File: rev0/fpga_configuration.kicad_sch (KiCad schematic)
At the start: 40 parts, among them IC1 ECP5-BGA256, J10 TC_SWD, J5 Conn_FPGA_JTAG_10, J6 Conn_ARM_JTAG_SWD_10, U6 ATSAMD11D14A-MUT, U7 W25Q32JVSS

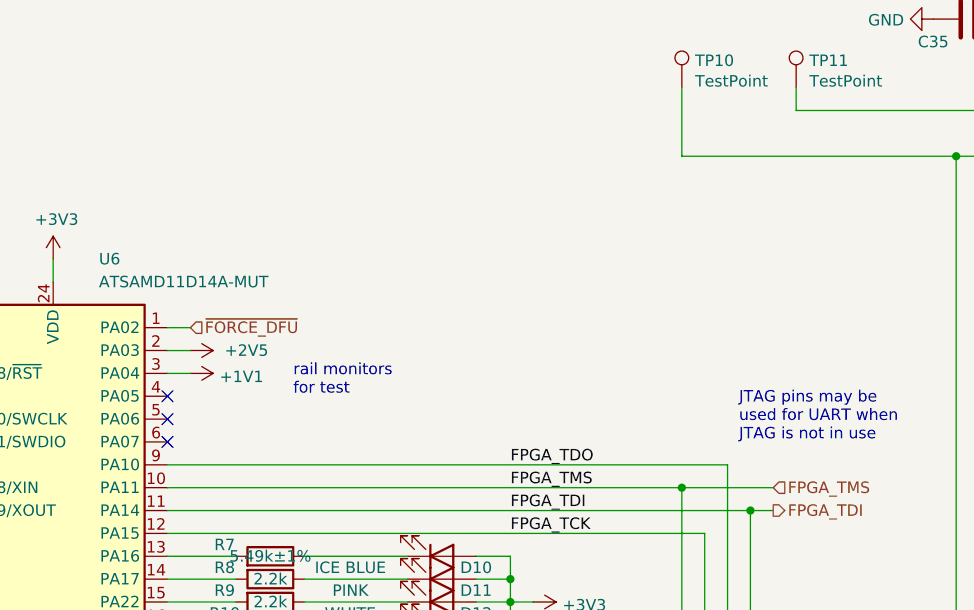
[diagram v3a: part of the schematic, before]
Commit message: hardware: add pin strap for version detection
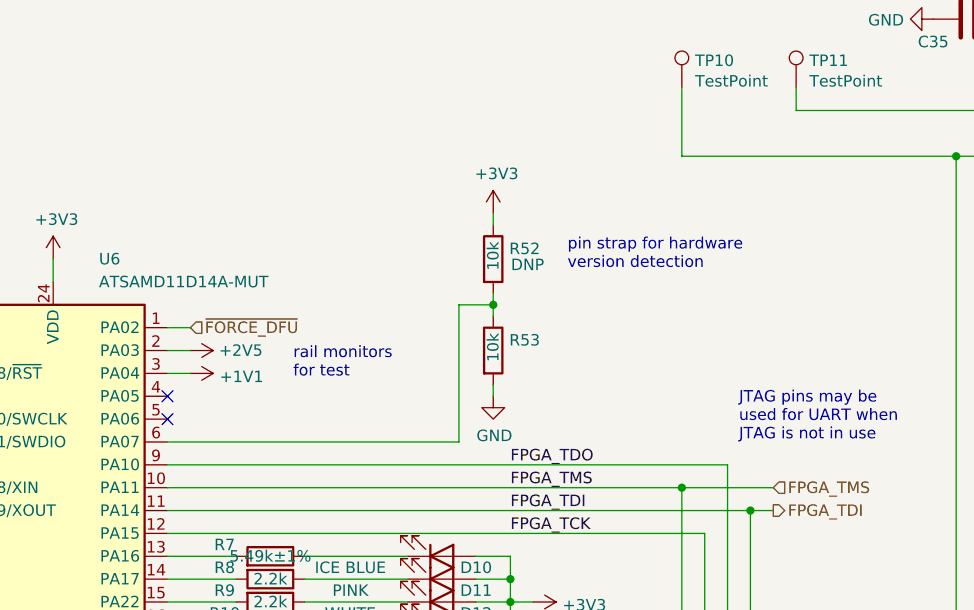
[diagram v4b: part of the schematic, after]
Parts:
- added R52, R53: 10k, Resistor_SMD:R_0402_1005Metric, symbol Device:R
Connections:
- net +3V3: now also R52.1
- net GND: now also R53.2
- net at U6.6 (PA07): now also R52.2, R53.1
- no-connect marks 13 -> 12
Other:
- note added: "pin strap for hardware version detection"
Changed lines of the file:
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@@
   (junction (at 195.58 35.56) (diameter 0) (color 0 0 0 0)
+  )
+  (junction (at 141.605 57.15) (diameter 0) (color 0 0 0 0)
   )
   (junction (at 138.43 187.96) (diameter 0) (color 0 0 0 0)
@@
   (no_connect (at 247.65 73.66))
   (no_connect (at 50.8 173.99))
-  (no_connect (at 105.41 72.39))
   (no_connect (at 50.8 176.53))
   (no_connect (at 123.19 162.56))
@@
     (stroke (width 0) (type default) (color 0 0 0 0))
   )
+  (wire (pts (xy 141.605 67.31) (xy 141.605 66.04))
+    (stroke (width 0) (type default) (color 0 0 0 0))
+  )
   (wire (pts (xy 64.77 107.95) (xy 64.77 110.49))
     (stroke (width 0) (type default) (color 0 0 0 0))
@@
     (stroke (width 0) (type default) (color 0 0 0 0))
   )
+  (wire (pts (xy 141.605 48.26) (xy 141.605 46.99))
+    (stroke (width 0) (type default) (color 0 0 0 0))
+  )
   (wire (pts (xy 92.71 52.07) (xy 92.71 54.61))
     (stroke (width 0) (type default) (color 0 0 0 0))
@@
     (stroke (width 0) (type default) (color 0 0 0 0))
   )
+  (wire (pts (xy 137.795 72.39) (xy 105.41 72.39))
+    (stroke (width 0) (type default) (color 0 0 0 0))
+  )
   (wire (pts (xy 105.41 90.17) (xy 113.03 90.17))
     (stroke (width 0) (type default) (color 0 0 0 0))
@@
     (stroke (width 0) (type default) (color 0 0 0 0))
   )
+  (wire (pts (xy 141.605 57.15) (xy 141.605 55.88))
+    (stroke (width 0) (type default) (color 0 0 0 0))
+  )
   (wire (pts (xy 233.68 128.27) (xy 247.65 128.27))
     (stroke (width 0) (type default) (color 0 0 0 0))
@@
     (stroke (width 0) (type default) (color 0 0 0 0))
   )
+  (wire (pts (xy 141.605 58.42) (xy 141.605 57.15))
+    (stroke (width 0) (type default) (color 0 0 0 0))
+  )
   (wire (pts (xy 71.12 36.83) (xy 71.12 39.37))
     (stroke (width 0) (type default) (color 0 0 0 0))
@@
     (stroke (width 0) (type default) (color 0 0 0 0))
   )
+  (wire (pts (xy 137.795 57.15) (xy 137.795 72.39))
+    (stroke (width 0) (type default) (color 0 0 0 0))
+  )
   (wire (pts (xy 33.02 171.45) (xy 50.8 171.45))
     (stroke (width 0) (type default) (color 0 0 0 0))
@@
   )
   (wire (pts (xy 33.02 62.23) (xy 33.02 64.77))
+    (stroke (width 0) (type default) (color 0 0 0 0))
+  )
+  (wire (pts (xy 141.605 57.15) (xy 137.795 57.15))
     (stroke (width 0) (type default) (color 0 0 0 0))
   )
@@
     (effects (font (size 1.27 1.27)) (justify left bottom))
   )
-  (text "rail monitors\nfor test" (at 119.38 67.31 0)
+  (text "rail monitors\nfor test" (at 119.38 65.405 0)
+    (effects (font (size 1.27 1.27)) (justify left bottom))
+  )
+  (text "pin strap for hardware\nversion detection" (at 149.86 53.34 0)
     (effects (font (size 1.27 1.27)) (justify left bottom))
   )
@@
       (effects (font (size 1.27 1.27)) hide)
     )
-    (property "Value" "+2V5" (id 1) (at 111.76 62.23 90)
+    (property "Value" "+2V5" (id 1) (at 111.125 62.23 90)
       (effects (font (size 1.27 1.27)) (justify left))
     )
@@
     (pin "1")
   )
+  (symbol (lib_id "power:+3V3") (at 141.605 46.99 0) (unit 1)
+    (in_bom yes) (on_board yes)
+    (property "Reference" "#PWR0138" (id 0) (at 141.605 50.8 0)
+      (effects (font (size 1.27 1.27)) hide)
+    )
+    (property "Value" "+3V3" (id 1) (at 141.986 42.5958 0))
+    (property "Footprint" "" (id 2) (at 141.605 46.99 0)
+      (effects (font (size 1.27 1.27)) hide)
+    )
+    (property "Datasheet" "" (id 3) (at 141.605 46.99 0)
+      (effects (font (size 1.27 1.27)) hide)
+    )
+    (pin "1")
+  )
+  (symbol (lib_id "power:GND") (at 141.605 67.31 0) (unit 1)
+    (in_bom yes) (on_board yes)
+    (property "Reference" "#PWR0139" (id 0) (at 141.605 73.66 0)
+      (effects (font (size 1.27 1.27)) hide)
+    )
+    (property "Value" "GND" (id 1) (at 141.732 71.7042 0))
+    (property "Footprint" "" (id 2) (at 141.605 67.31 0)
+      (effects (font (size 1.27 1.27)) hide)
+    )
+    (property "Datasheet" "" (id 3) (at 141.605 67.31 0)
+      (effects (font (size 1.27 1.27)) hide)
+    )
+    (pin "1")
+  )
+  (symbol (lib_id "Device:R") (at 141.605 62.23 0) (unit 1)
+    (in_bom yes) (on_board yes)
+    (property "Reference" "R53" (id 0) (at 143.383 61.087 0)
+      (effects (font (size 1.27 1.27)) (justify left))
+    )
+    (property "Value" "10k" (id 1) (at 141.605 63.5 90)
+      (effects (font (size 1.27 1.27)) (justify left))
+    )
+    (property "Footprint" "Resistor_SMD:R_0402_1005Metric" (id 2) (at 139.827 62.23 90)
+      (effects (font (size 1.27 1.27)) hide)
+    )
+    (property "Datasheet" "~" (id 3) (at 141.605 62.23 0)
+      (effects (font (size 1.27 1.27)) hide)
+    )
+    (property "Part Number" "GENERIC-RES-0402-10K" (id 4) (at 141.605 62.23 0)
+      (effects (font (size 1.27 1.27)) hide)
+    )
+    (property "Substitution" "any equivalent" (id 5) (at 141.605 62.23 0)
+      (effects (font (size 1.27 1.27)) hide)
+    )
+    (pin "1")
+    (pin "2")
+  )
+  (symbol (lib_id "Device:R") (at 141.605 52.07 0) (unit 1)
+    (in_bom yes) (on_board yes)
+    (property "Reference" "R52" (id 0) (at 143.383 50.927 0)
+      (effects (font (size 1.27 1.27)) (justify left))
+    )
+    (property "Value" "10k" (id 1) (at 141.605 53.34 90)
+      (effects (font (size 1.27 1.27)) (justify left))
+    )
+    (property "Footprint" "Resistor_SMD:R_0402_1005Metric" (id 2) (at 139.827 52.07 90)
+      (effects (font (size 1.27 1.27)) hide)
+    )
+    (property "Datasheet" "~" (id 3) (at 141.605 52.07 0)
+      (effects (font (size 1.27 1.27)) hide)
+    )
+    (property "Part Number" "GENERIC-RES-0402-10K" (id 4) (at 141.605 52.07 0)
+      (effects (font (size 1.27 1.27)) hide)
+    )
+    (property "Substitution" "any equivalent" (id 5) (at 141.605 52.07 0)
+      (effects (font (size 1.27 1.27)) hide)
+    )
+    (property "DNP" "DNP" (id 6) (at 145.415 52.705 0))
+    (pin "1")
+    (pin "2")
+  )
 )

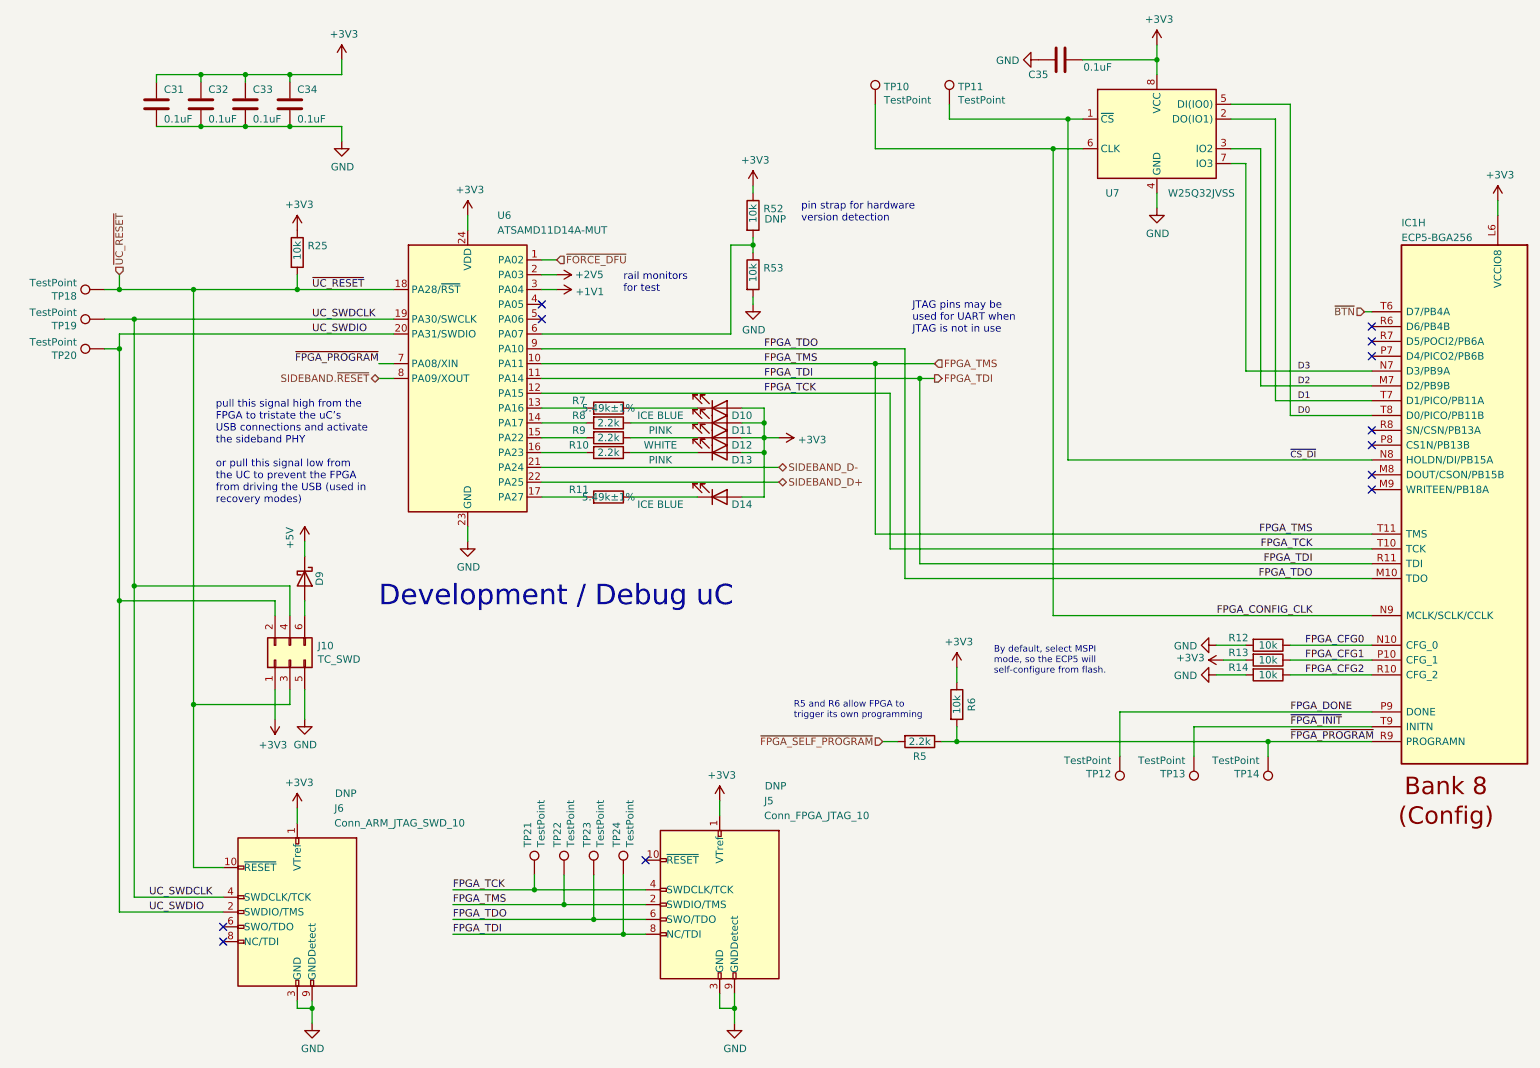
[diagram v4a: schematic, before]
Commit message: hardware: add FPGA interrupt
allows FPGA to signal that it has something to say to the
microcontroller
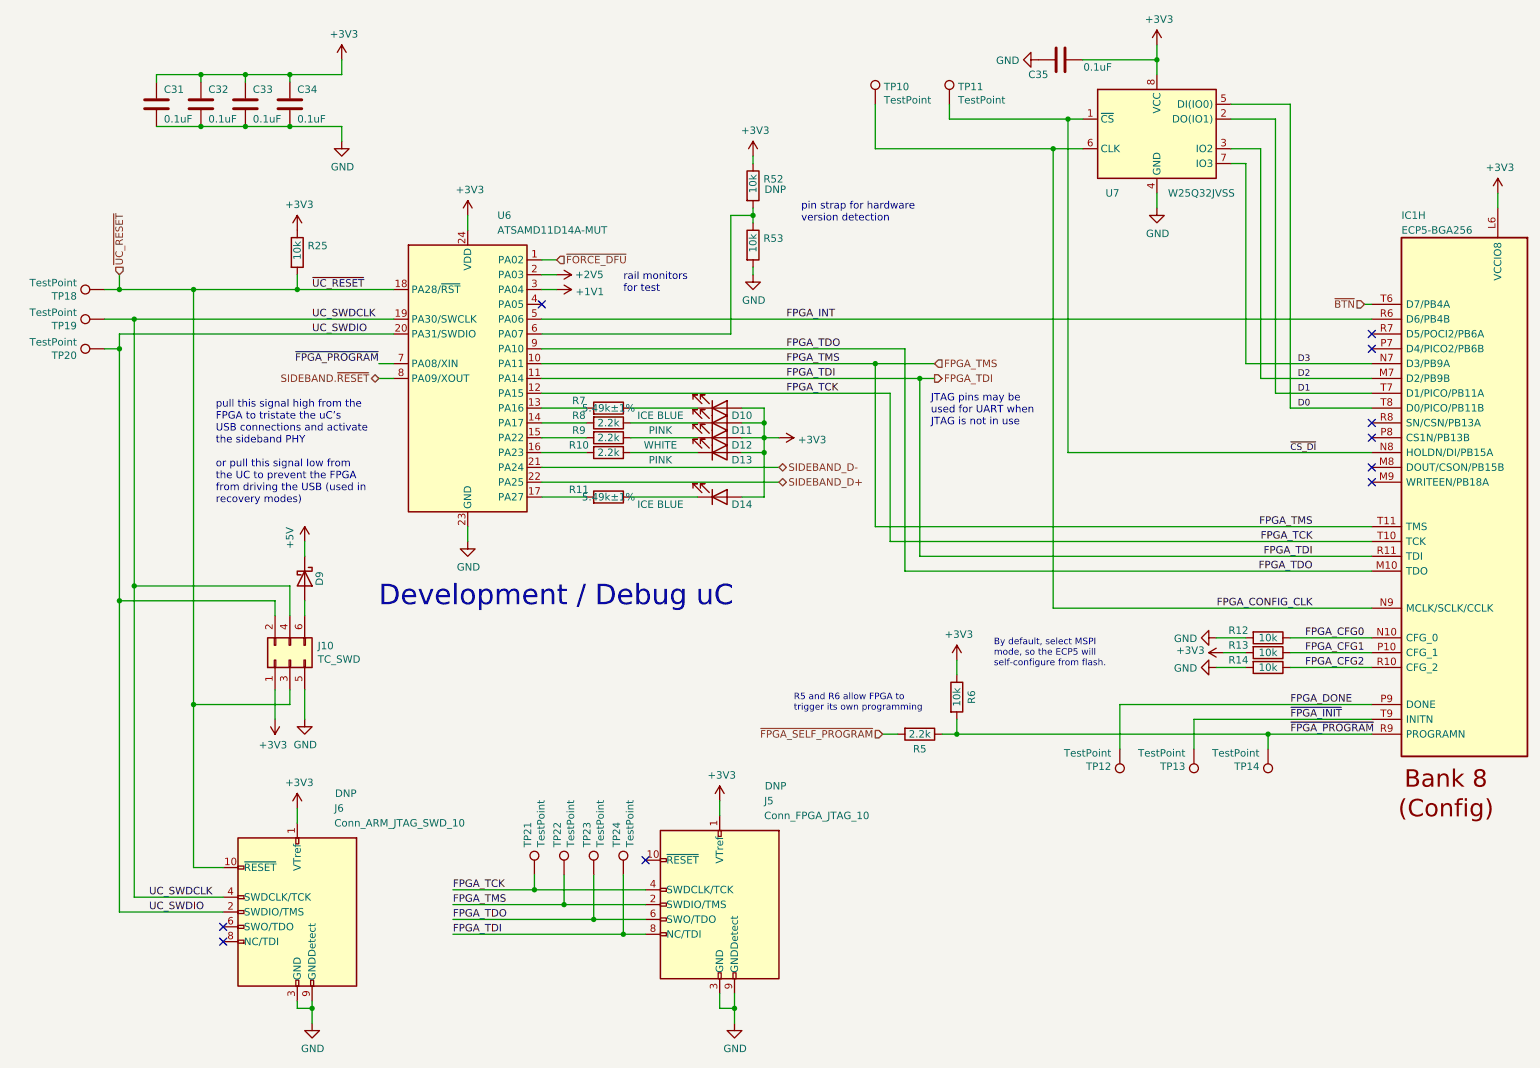
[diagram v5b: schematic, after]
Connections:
- net FPGA_INT: now reaches IC1.R6 (D6/PB4B)
- net FPGA_INT: now also U6.5 (PA06)
- no-connect marks 12 -> 10
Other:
- moved on the sheet: IC1H, R12, R13, R14, R5, R52, R53, R6, TP12, TP13, TP14

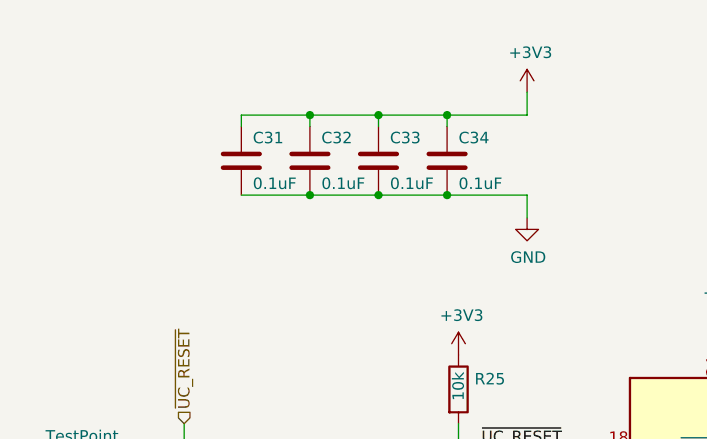
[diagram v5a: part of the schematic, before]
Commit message: hardware: restore 1.8 V RAM supply as an option
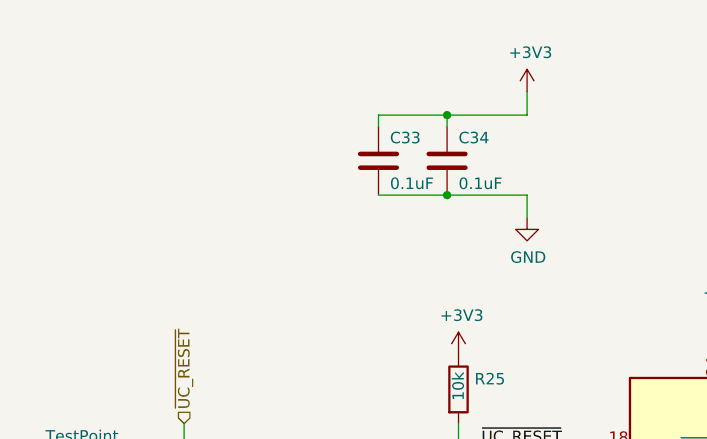
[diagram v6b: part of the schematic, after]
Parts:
- removed C31, C32: 0.1uF, Capacitor_SMD:C_0402_1005Metric, symbol Device:C
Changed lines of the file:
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@@
   (junction (at 229.87 140.97) (diameter 0) (color 0 0 0 0)
   )
-  (junction (at 54.61 36.83) (diameter 0) (color 0 0 0 0)
-  )
   (junction (at 33.02 64.77) (diameter 0) (color 0 0 0 0)
   )
@@
   (junction (at 33.02 118.11) (diameter 0) (color 0 0 0 0)
   )
-  (junction (at 46.99 36.83) (diameter 0) (color 0 0 0 0)
-  )
   (junction (at 210.82 25.4) (diameter 0) (color 0 0 0 0)
   )
   (junction (at 63.5 64.77) (diameter 0) (color 0 0 0 0)
   )
-  (junction (at 54.61 27.94) (diameter 0) (color 0 0 0 0)
-  )
   (junction (at 143.51 87.63) (diameter 0) (color 0 0 0 0)
   )
@@
   )
   (junction (at 45.72 64.77) (diameter 0) (color 0 0 0 0)
-  )
-  (junction (at 46.99 27.94) (diameter 0) (color 0 0 0 0)
   )
   (junction (at 45.72 135.89) (diameter 0) (color 0 0 0 0)
@@
     (stroke (width 0) (type default) (color 0 0 0 0))
   )
-  (wire (pts (xy 46.99 29.21) (xy 46.99 27.94))
-    (stroke (width 0) (type default) (color 0 0 0 0))
-  )
   (wire (pts (xy 109.22 165.1) (xy 109.22 170.18))
     (stroke (width 0) (type default) (color 0 0 0 0))
@@
     (stroke (width 0) (type default) (color 0 0 0 0))
   )
-  (wire (pts (xy 39.37 36.83) (xy 46.99 36.83))
-    (stroke (width 0) (type default) (color 0 0 0 0))
-  )
   (wire (pts (xy 119.38 175.26) (xy 90.17 175.26))
     (stroke (width 0) (type default) (color 0 0 0 0))
@@
     (stroke (width 0) (type default) (color 0 0 0 0))
   )
-  (wire (pts (xy 46.99 36.83) (xy 54.61 36.83))
-    (stroke (width 0) (type default) (color 0 0 0 0))
-  )
   (wire (pts (xy 132.08 87.63) (xy 120.65 87.63))
     (stroke (width 0) (type default) (color 0 0 0 0))
   )
-  (wire (pts (xy 54.61 27.94) (xy 46.99 27.94))
-    (stroke (width 0) (type default) (color 0 0 0 0))
-  )
   (wire (pts (xy 143.51 90.17) (xy 143.51 87.63))
     (stroke (width 0) (type default) (color 0 0 0 0))
@@
     (stroke (width 0) (type default) (color 0 0 0 0))
   )
-  (wire (pts (xy 39.37 29.21) (xy 39.37 27.94))
-    (stroke (width 0) (type default) (color 0 0 0 0))
-  )
   (wire (pts (xy 247.65 77.47) (xy 226.06 77.47))
     (stroke (width 0) (type default) (color 0 0 0 0))
@@
   )
   (wire (pts (xy 141.605 52.07) (xy 137.795 52.07))
-    (stroke (width 0) (type default) (color 0 0 0 0))
-  )
-  (wire (pts (xy 39.37 27.94) (xy 46.99 27.94))
     (stroke (width 0) (type default) (color 0 0 0 0))
   )
@@
     (pin "1")
   )
-  (symbol (lib_id "Device:C") (at 46.99 33.02 0) (unit 1)
-    (in_bom yes) (on_board yes)
-    (property "Reference" "C32" (id 0) (at 48.26 30.48 0)
-      (effects (font (size 1.27 1.27)) (justify left))
-    )
-    (property "Value" "0.1uF" (id 1) (at 48.26 35.56 0)
-      (effects (font (size 1.27 1.27)) (justify left))
-    )
-    (property "Footprint" "Capacitor_SMD:C_0402_1005Metric" (id 2) (at 47.9552 36.83 0)
-      (effects (font (size 1.27 1.27)) hide)
-    )
-    (property "Datasheet" "~" (id 3) (at 46.99 33.02 0)
-      (effects (font (size 1.27 1.27)) hide)
-    )
-    (property "Part Number" "GENERIC-CAP-0402-0.1uF" (id 4) (at 46.99 33.02 0)
-      (effects (font (size 1.27 1.27)) hide)
-    )
-    (property "Substitution" "any equivalent" (id 5) (at 46.99 33.02 0)
-      (effects (font (size 1.27 1.27)) hide)
-    )
-    (pin "1")
-    (pin "2")
-  )
   (symbol (lib_id "Device:C") (at 54.61 33.02 0) (unit 1)
     (in_bom yes) (on_board yes)
@@
       (effects (font (size 1.27 1.27)) hide)
     )
-    (pin "1")
-    (pin "2")
-  )
-  (symbol (lib_id "Device:C") (at 39.37 33.02 0) (unit 1)
-    (in_bom yes) (on_board yes)
-    (property "Reference" "C31" (id 0) (at 40.64 30.48 0)
-      (effects (font (size 1.27 1.27)) (justify left))
-    )
-    (property "Value" "0.1uF" (id 1) (at 40.64 35.56 0)
-      (effects (font (size 1.27 1.27)) (justify left))
-    )
-    (property "Footprint" "Capacitor_SMD:C_0402_1005Metric" (id 2) (at 40.3352 36.83 0)
-      (effects (font (size 1.27 1.27)) hide)
-    )
-    (property "Datasheet" "~" (id 3) (at 39.37 33.02 0)
-      (effects (font (size 1.27 1.27)) hide)
-    )
-    (property "Part Number" "GENERIC-CAP-0402-0.1uF" (id 4) (at 39.37 33.02 0)
-      (effects (font (size 1.27 1.27)) hide)
-    )
-    (property "Substitution" "any equivalent" (id 5) (at 39.37 33.02 0)
-      (effects (font (size 1.27 1.27)) hide)
-    )
